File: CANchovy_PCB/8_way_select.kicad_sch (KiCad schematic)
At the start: 8 parts

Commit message: Revision C & readme updates.
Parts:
- JP1: value OPT_4 -> OPT_5
- JP1: value OPT_2 -> OPT_7
- JP1: value OPT_1 -> OPT_8
- JP1: value OPT_3 -> OPT_6
- JP2: value OPT_5 -> OPT_4
- JP3: value OPT_6 -> OPT_3
- JP4: value OPT_7 -> OPT_2
- JP5: value OPT_8 -> OPT_1
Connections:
- net OPT_1: now also JP5.1 (A); no longer JP1.1 (A)
- net OPT_2: now also JP4.1 (A); no longer JP1.1 (A)
- net OPT_3: now also JP3.1 (A); no longer JP1.1 (A)
- net OPT_4: now also JP2.1 (A); no longer JP1.1 (A)
- net OPT_5: now also JP1.1 (A); no longer JP2.1 (A)
- net OPT_6: now also JP1.1 (A); no longer JP3.1 (A)
- net OPT_7: now also JP1.1 (A); no longer JP4.1 (A)
- net OPT_8: now also JP1.1 (A); no longer JP5.1 (A)
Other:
- moved on the sheet: JP1, JP2, JP3, JP4, JP5

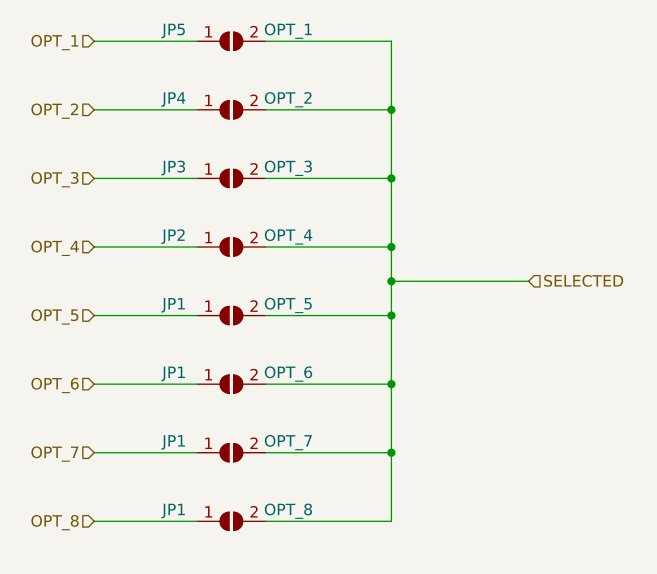
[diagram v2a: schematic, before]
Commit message: Release V1.0
Green LED D3 changed to C965804.
Blue LED D2 changed to C965807.
README edits.
Design files updated to KiCAD V8 format.
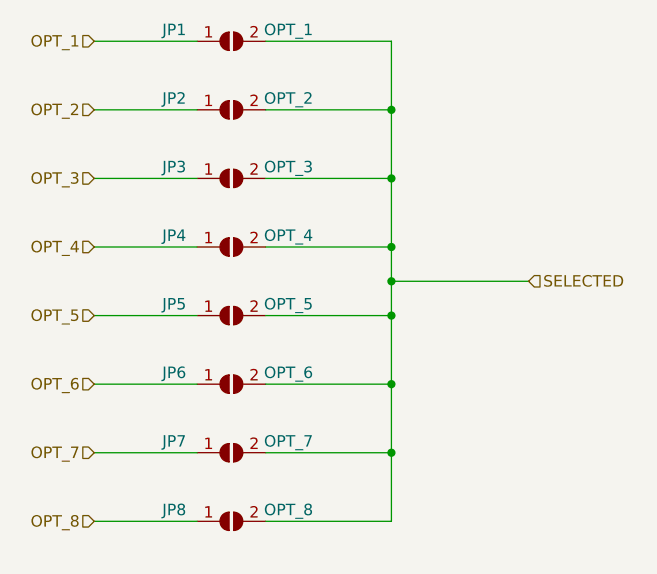
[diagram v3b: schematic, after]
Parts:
- renumbered JP5 to JP1, JP4 to JP2, JP2 to JP4, JP1 to JP5, JP1 to JP6, JP1 to JP7, JP1 to JP8
